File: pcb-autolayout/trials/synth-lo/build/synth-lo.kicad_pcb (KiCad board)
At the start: 4 copper layers, 70 x 50 mm, 44 parts, among them J1 CONN, U1 MCU, U11 BUF, U12 BUF, U13 BUF, U14 BUF, U15 BUF, U16 BUF, U2 LDO, Y1 8MHz

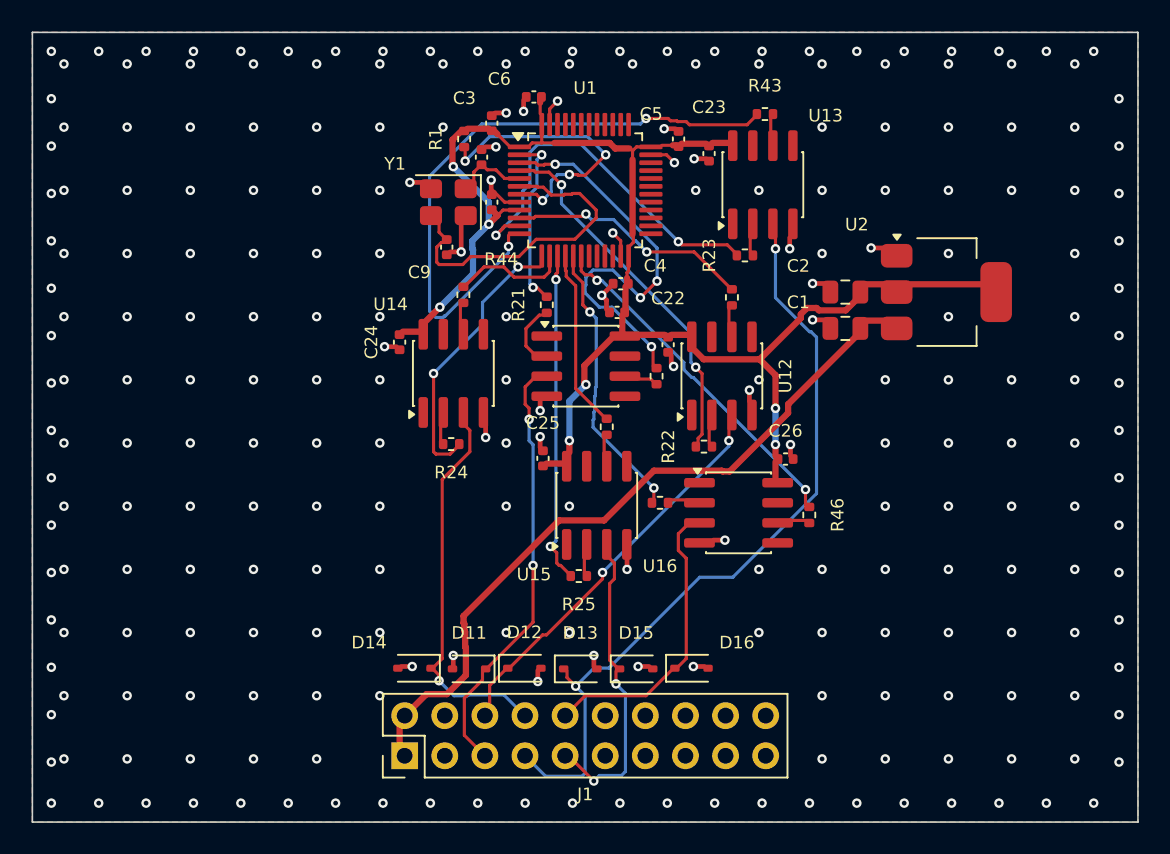
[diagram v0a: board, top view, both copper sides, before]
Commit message: synth-lo: build của lượt bench (1 chân hở — hồi quy đang truy)
Co-Authored-By: Claude Opus 5.5 <noreply@anthropic.com>
Claude-Session: https://claude.ai/code/session_012jwodCpQFB8wopi3P3TnUz
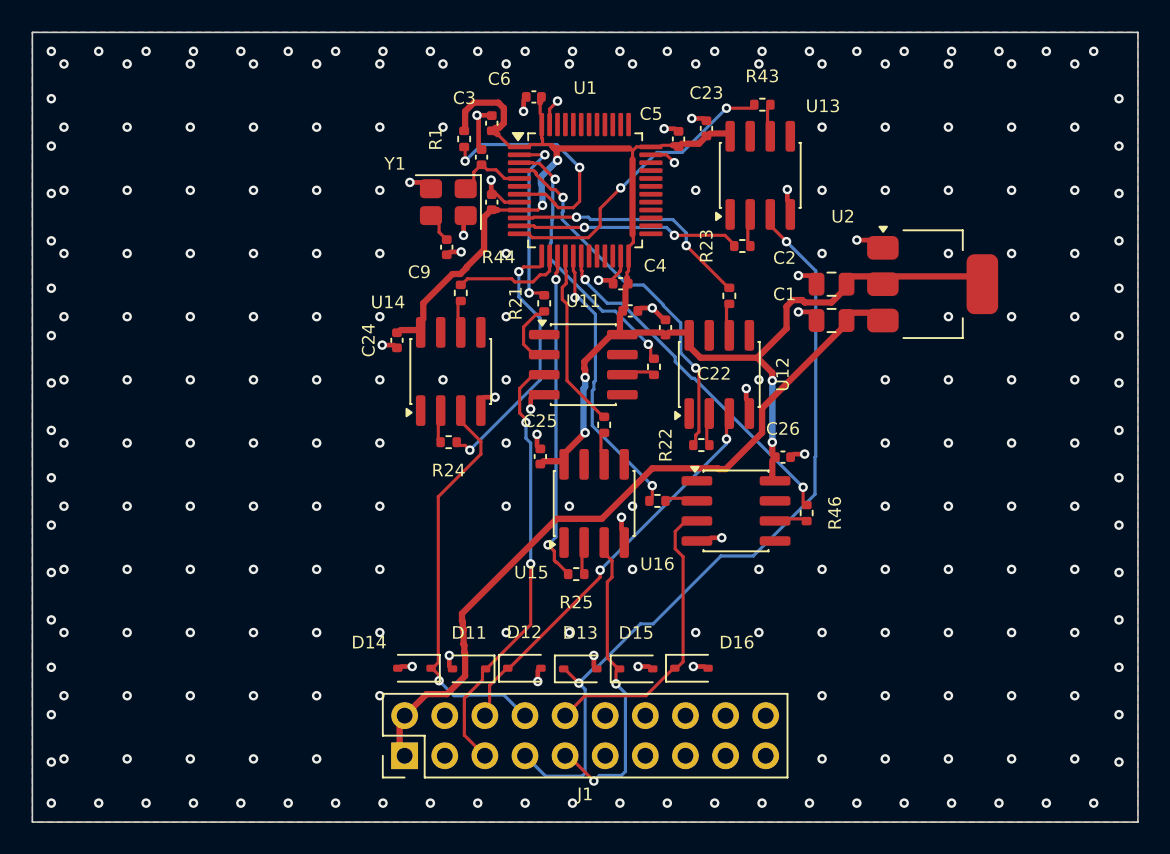
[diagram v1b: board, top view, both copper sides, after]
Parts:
- moved C4 1.83 mm to (137.2, 75.9)
- moved C21 1.83 mm to (137.9, 77.6), turned to 0 degrees
- moved C23 1.60 mm to (142.7, 66.1), turned to 90 degrees
- moved C22 1.11 mm to (140.1, 78.7), turned to 90 degrees
- moved C1 1.01 mm to (150.6, 78.2)
- moved C2 1.01 mm to (150.6, 75.9)
- moved U2 1.01 mm to (157.0, 75.9)
- moved R41 0.62 mm to (139.4, 81.2)
- moved R23 0.62 mm to (144.9, 73.5)
- moved R43 0.62 mm to (146.2, 64.6)
- moved U13 0.62 mm to (146.1, 69.1)
- moved C25 0.20 mm to (132.2, 86.9)
- moved R45 0.20 mm to (136.2, 84.9)
- moved U15 0.20 mm to (135.6, 89.8)
- moved R25 0.20 mm to (134.4, 94.3)
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- renumbered C4 to C21, C21 to C4
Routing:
- net S3_B: track 38.9 -> 18.2 mm
- net OSC_OUT: track 19.4 -> 1.07 mm
- net S3_A: track 23.2 -> 13.2 mm
- net S1_B: track 26.1 -> 16.5 mm, vias 4 -> 2
- net NRST: track 17.4 -> 14.9 mm, vias 4 -> 2
- net +3V3: track 80.3 -> 82.5 mm, vias 7 -> 6
- net GND: track 28.4 -> 29.6 mm, vias 249 -> 254
- net S4_A: track 17.0 -> 16.0 mm
- net S4_OUT: track 22.9 -> 23.7 mm
- net S1_A: track 10.4 -> 10.9 mm

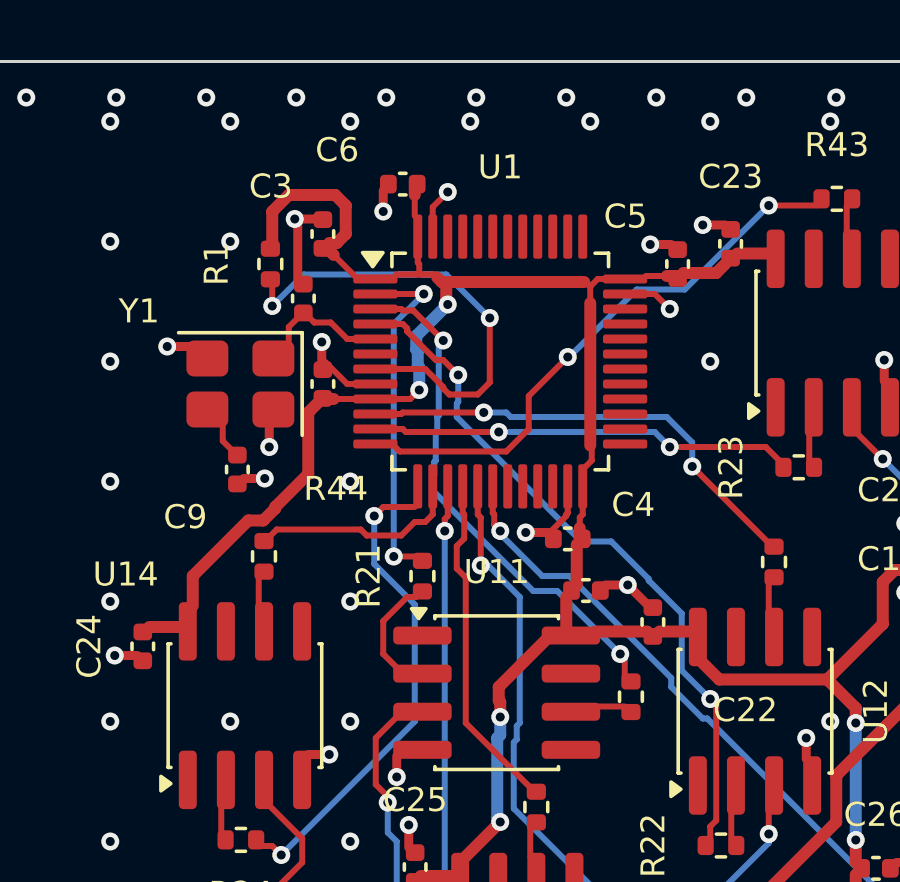
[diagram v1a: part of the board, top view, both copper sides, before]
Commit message: bench: STALL 10 sửa hồi quy synth-lo (16/16, 225 s); baseline 2 trung thực (synth-hi 2 hở, DRC 0)
Co-Authored-By: Claude Opus 5.5 <noreply@anthropic.com>
Claude-Session: https://claude.ai/code/session_012jwodCpQFB8wopi3P3TnUz
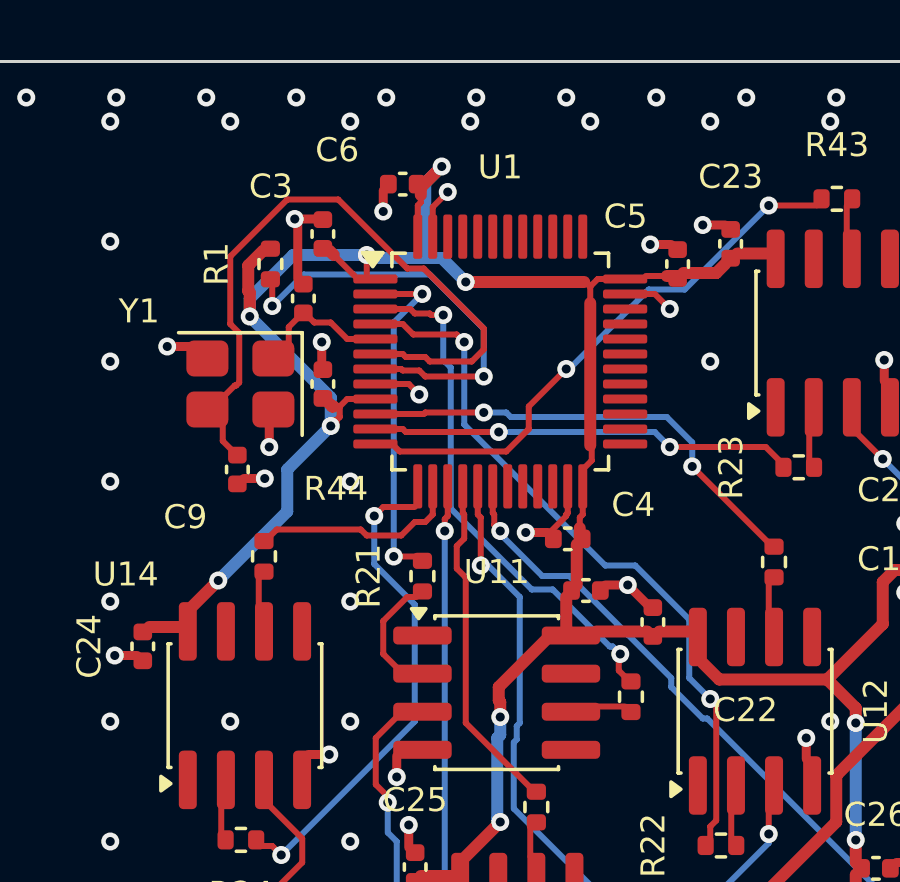
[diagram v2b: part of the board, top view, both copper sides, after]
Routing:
- net OSC_OUT: track 1.07 -> 21.1 mm
- net +3V3: track 82.5 -> 90.0 mm, vias 6 -> 10
- net NRST: track 14.9 -> 13.6 mm
- net GND: track 29.6 -> 28.5 mm
- net S2_A: track 22.6 -> 23.2 mm
